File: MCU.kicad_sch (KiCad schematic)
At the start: 8 parts, among them J6 Conn_02x07_Odd_Even, U10 STM32H723VGTx, Y1 Resonator

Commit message: change cad data
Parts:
- added C15: 0.1μF, Capacitor_SMD:C_0603_1608Metric_Pad1.08x0.95mm_HandSolder, symbol Device:C
- added C47, C49, C50: 0.1uF, Capacitor_SMD:C_0402_1005Metric_Pad0.74x0.62mm_HandSolder, symbol Device:C
- added D7: WS2812B, LED_SMD:LED_WS2812B_PLCC4_5.0x5.0mm_P3.2mm, symbol LED:WS2812B
- added FB2: FerriteBead, Inductor_SMD:L_0603_1608Metric_Pad1.05x0.95mm_HandSolder, symbol Device:FerriteBead
- added R70: 12kΩ, Resistor_SMD:R_0603_1608Metric_Pad0.98x0.95mm_HandSolder, symbol Device:R
- added SW3: SW_Push, Button_Switch_SMD:SW_Push_1P1T_NO_CK_KMR2, symbol Switch:SW_Push
- Y2: renamed from Y1; value Resonator -> 16Mhz
- renumbered C33 to C46, C35 to C53, C36 to C54, C41 to C59, C34 to C61, U10 to U11
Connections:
- net +3.3V: now also U11.6 (VBAT), C47.1, D7.1 (VDD), FB2.1
- net CAN1RX: now also U11.81 (PD0); no longer U11.70 (PA11)
- net CAN1TX: now also U11.82 (PD1); no longer U11.71 (PA12)
- net GND: now also C15.2, C47.2, C49.2, C50.2, D7.3 (VSS), R70.1, SW3.1
- net NRST: now also C15.1, SW3.2
- net SCLK: now reaches U11.1 (PE2)
- net at U11.20 (VREF+): now also C50.1
- net VDDA: now reaches U11.21 (VDDA)
- net VDDA: now also C49.1, FB2.2
- net CS: now reaches U11.3 (PE4)
- net MISO: now reaches U11.4 (PE5)
- net MOSI: now reaches U11.5 (PE6)
- net LED: now reaches U11.67 (PA8)
- net LED: now also D7.4 (DIN)
- net at U11.94 (BOOT0): now also R70.2
- net INT: now reaches U11.97 (PE0)
- net RST: now reaches U11.98 (PE1)
- new net USB_DN: U11.70 (PA11)
- new net USB_DP: U11.71 (PA12)
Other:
- moved on the sheet: J6

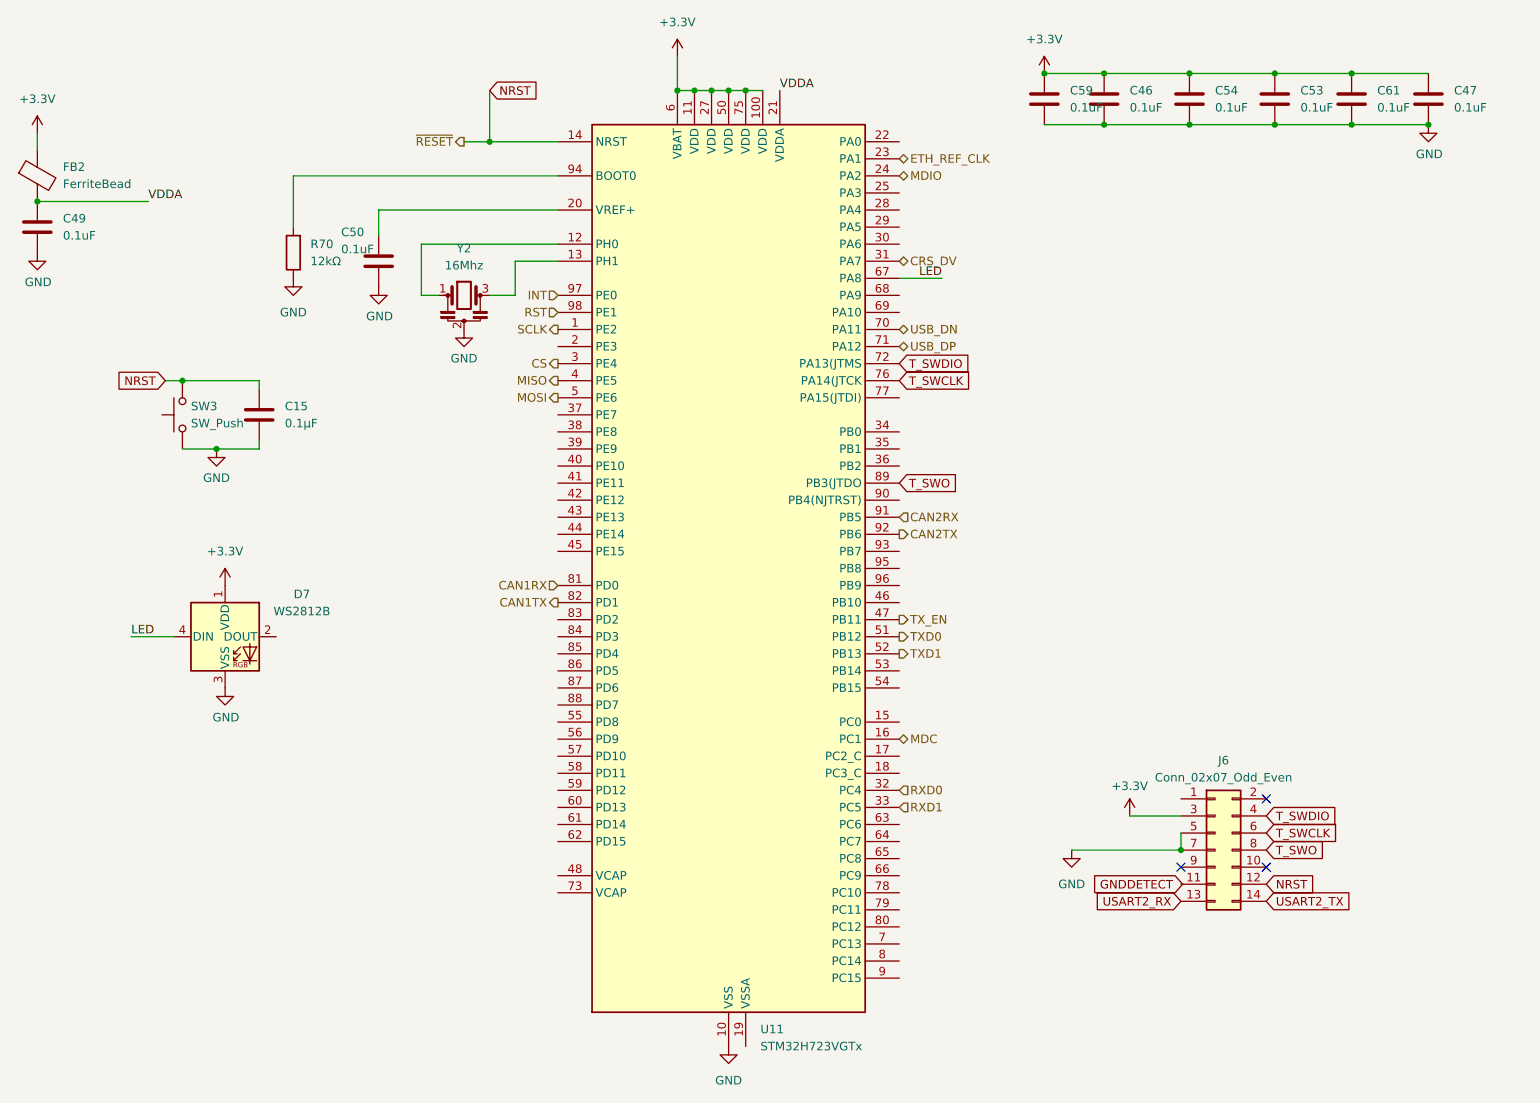
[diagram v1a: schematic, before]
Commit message: remove efuse
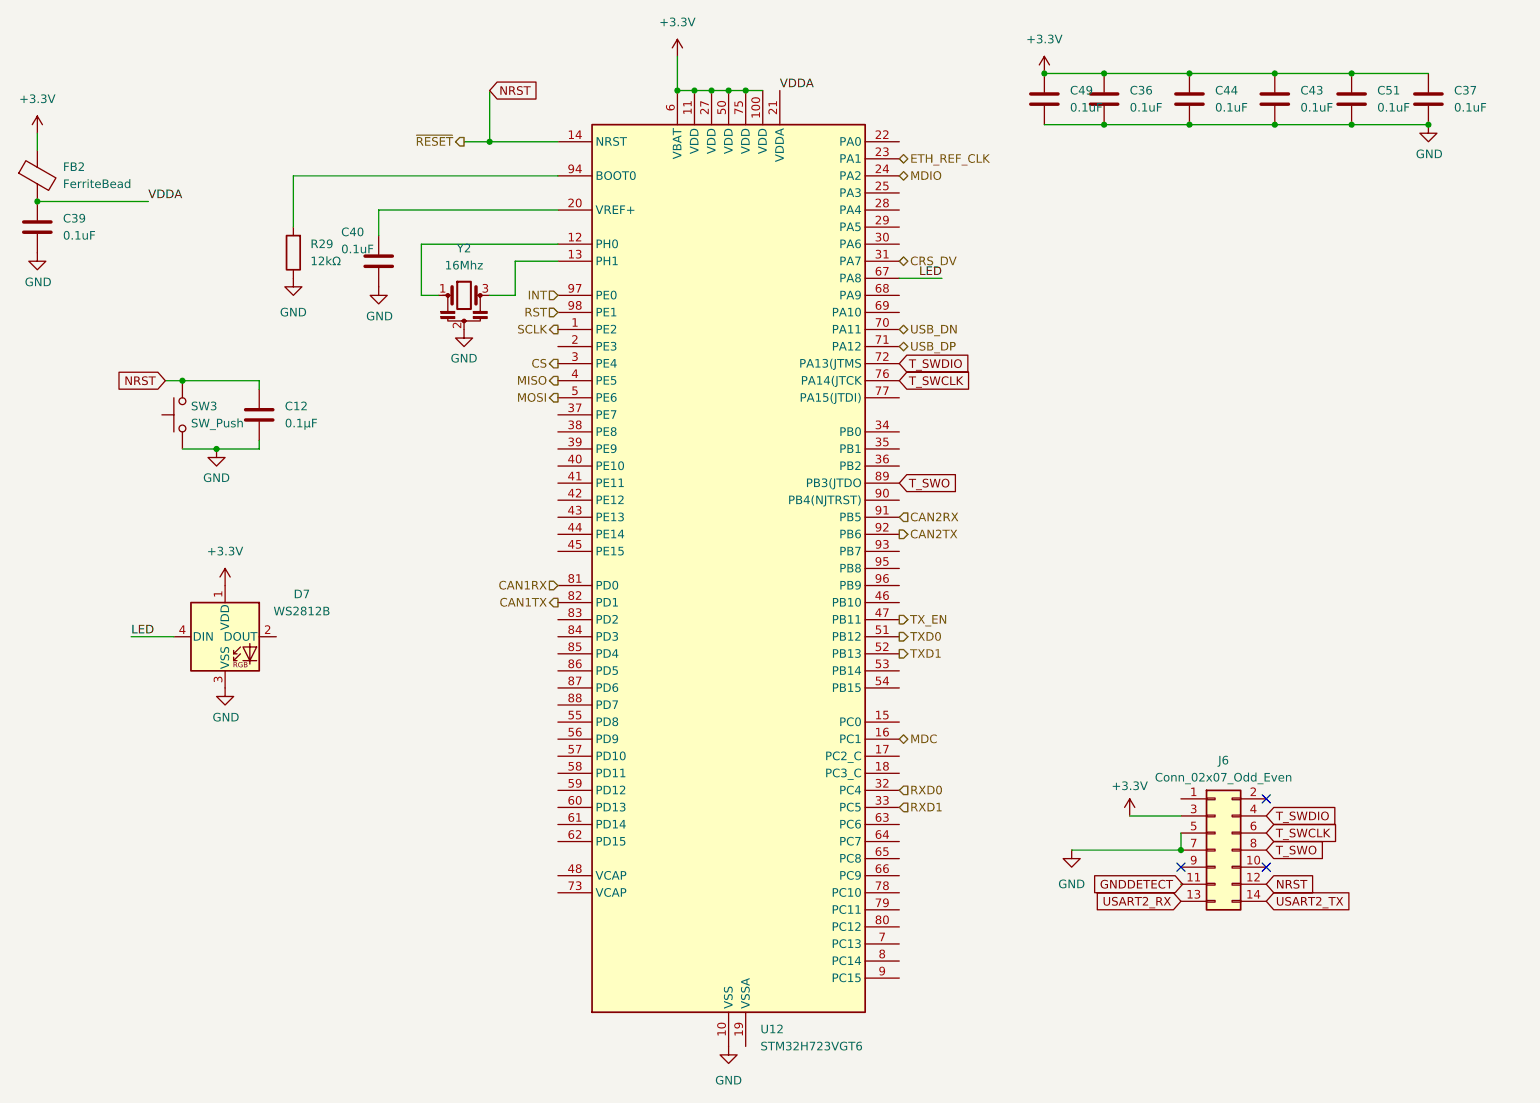
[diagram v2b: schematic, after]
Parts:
- U12: renamed from U11; value STM32H723VGTx -> STM32H723VGT6
- Y2: footprint Crystal:Resonator_SMD_Murata_CSTxExxV-3Pin_3.0x1.1mm_HandSoldering -> Crystal:Resonator_SMD_Murata_CSTxExxV-3Pin_3.0x1.1mm
- renumbered C15 to C12, C46 to C36, C47 to C37, C49 to C39, C50 to C40, C53 to C43, C54 to C44, C59 to C49, C61 to C51, R70 to R29

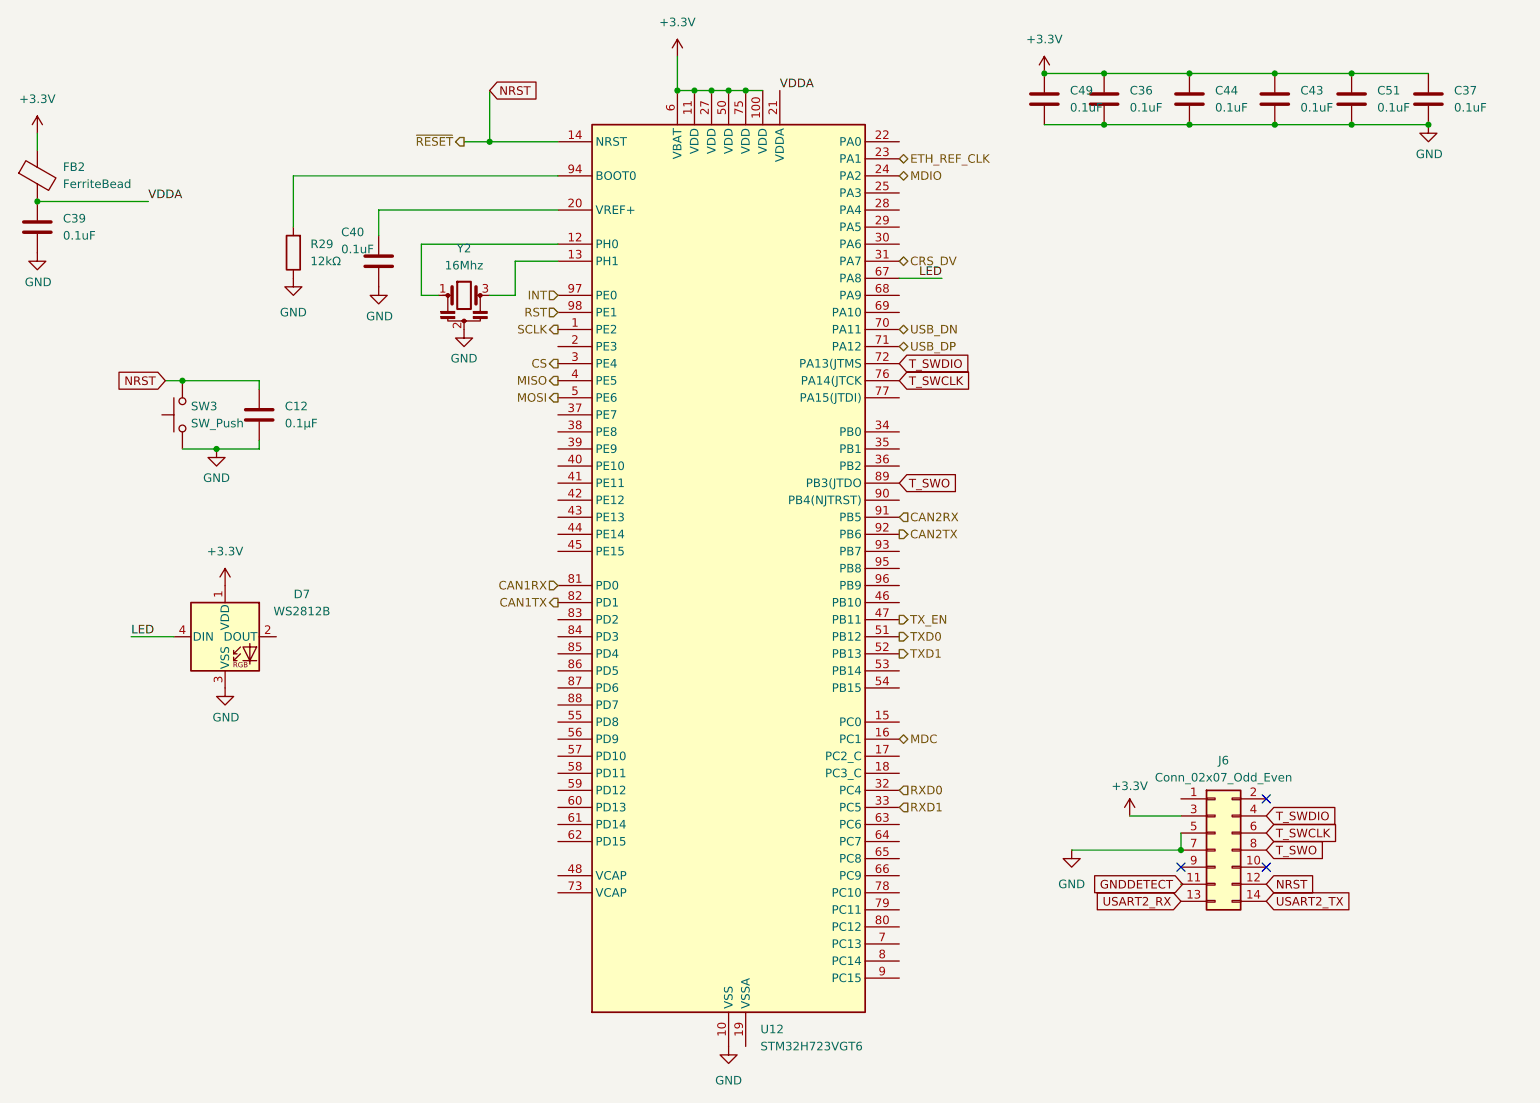
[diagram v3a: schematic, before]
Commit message: add sata capacitor
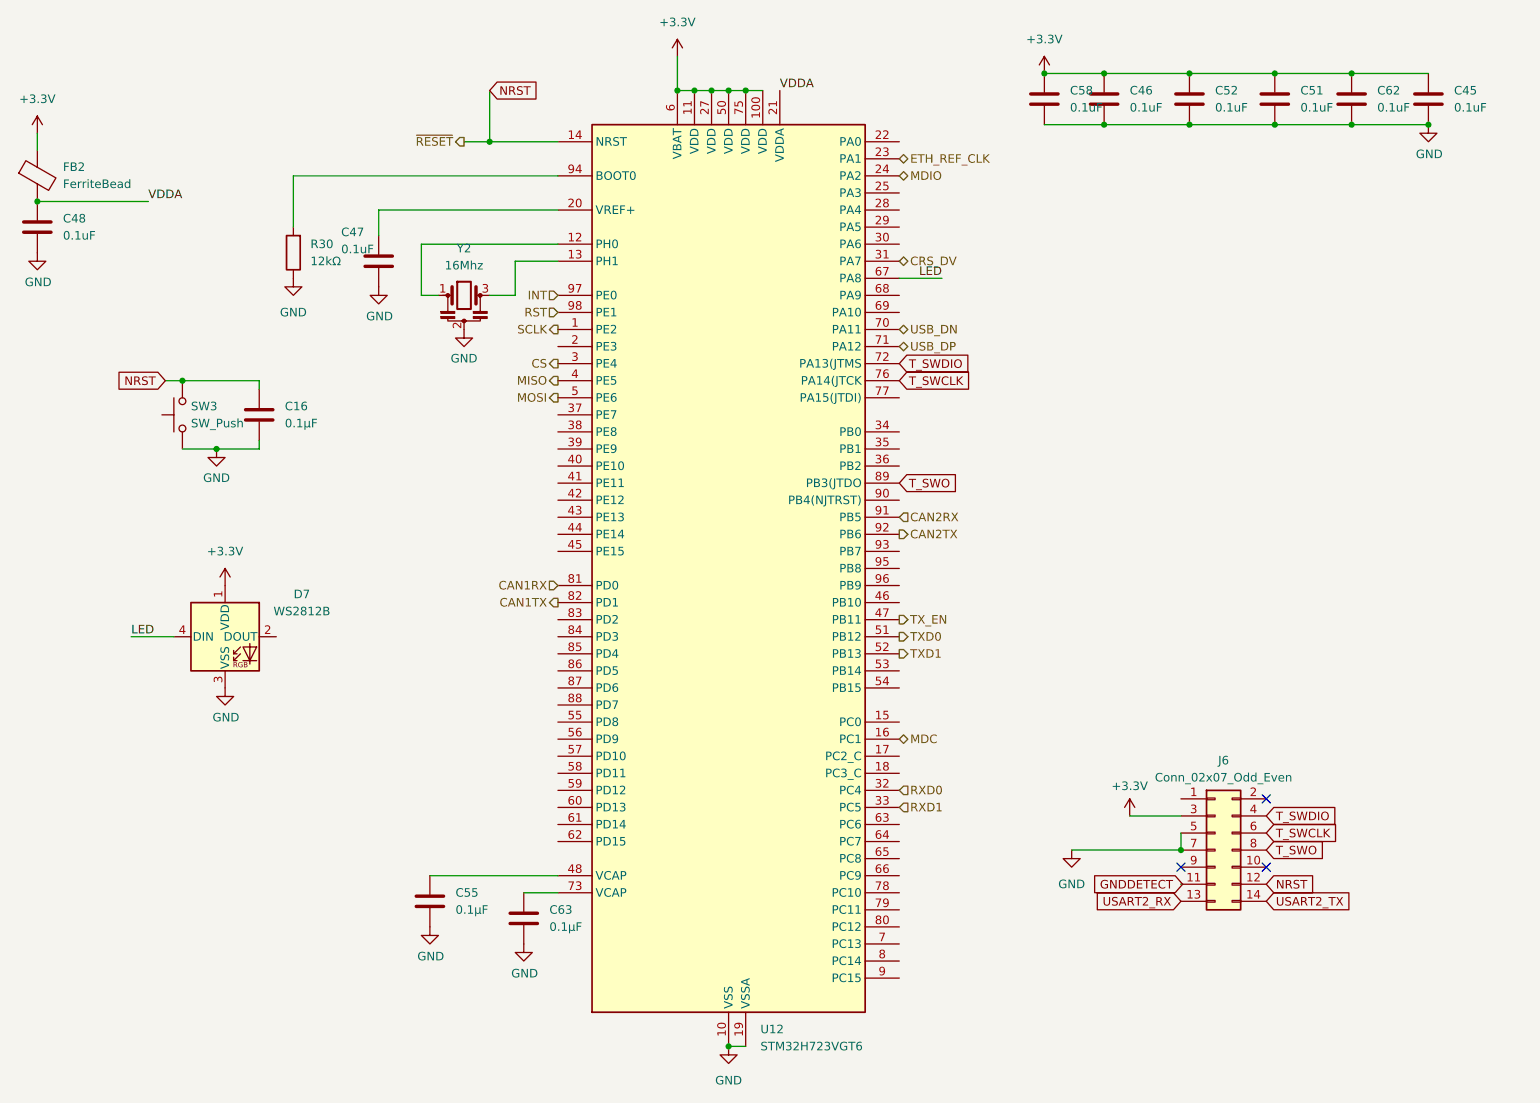
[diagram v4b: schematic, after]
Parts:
- added C55, C63: 0.1μF, Capacitor_SMD:C_0402_1005Metric_Pad0.74x0.62mm_HandSolder, symbol Device:C
- renumbered C12 to C16, C37 to C45, C36 to C46, C40 to C47, C39 to C48, C43 to C51, C44 to C52, C49 to C58, C51 to C62, R29 to R30
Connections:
- net GND: now also U12.19 (VSSA), C55.2, C63.2
- net at U12.48 (VCAP): now also C55.1
- net at U12.73 (VCAP): now also C63.1

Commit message: add logp
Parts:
- renumbered R30 to R27

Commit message: end route
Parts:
- renumbered FB2 to FB1
